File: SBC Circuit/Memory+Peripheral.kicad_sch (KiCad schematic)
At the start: 15 parts, among them U11 MCM6206CP, U12 28C256, U13 MCM6206CP, U14 28C256, U2 68681

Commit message: Small changes to prepare for review
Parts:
- renumbered C15 to C1, C16 to C2, C17 to C3, C18 to C4, C19 to C5, C20 to C6, C21 to C7, C22 to C8, U11 to U4, U12 to U5, U13 to U6, U14 to U7

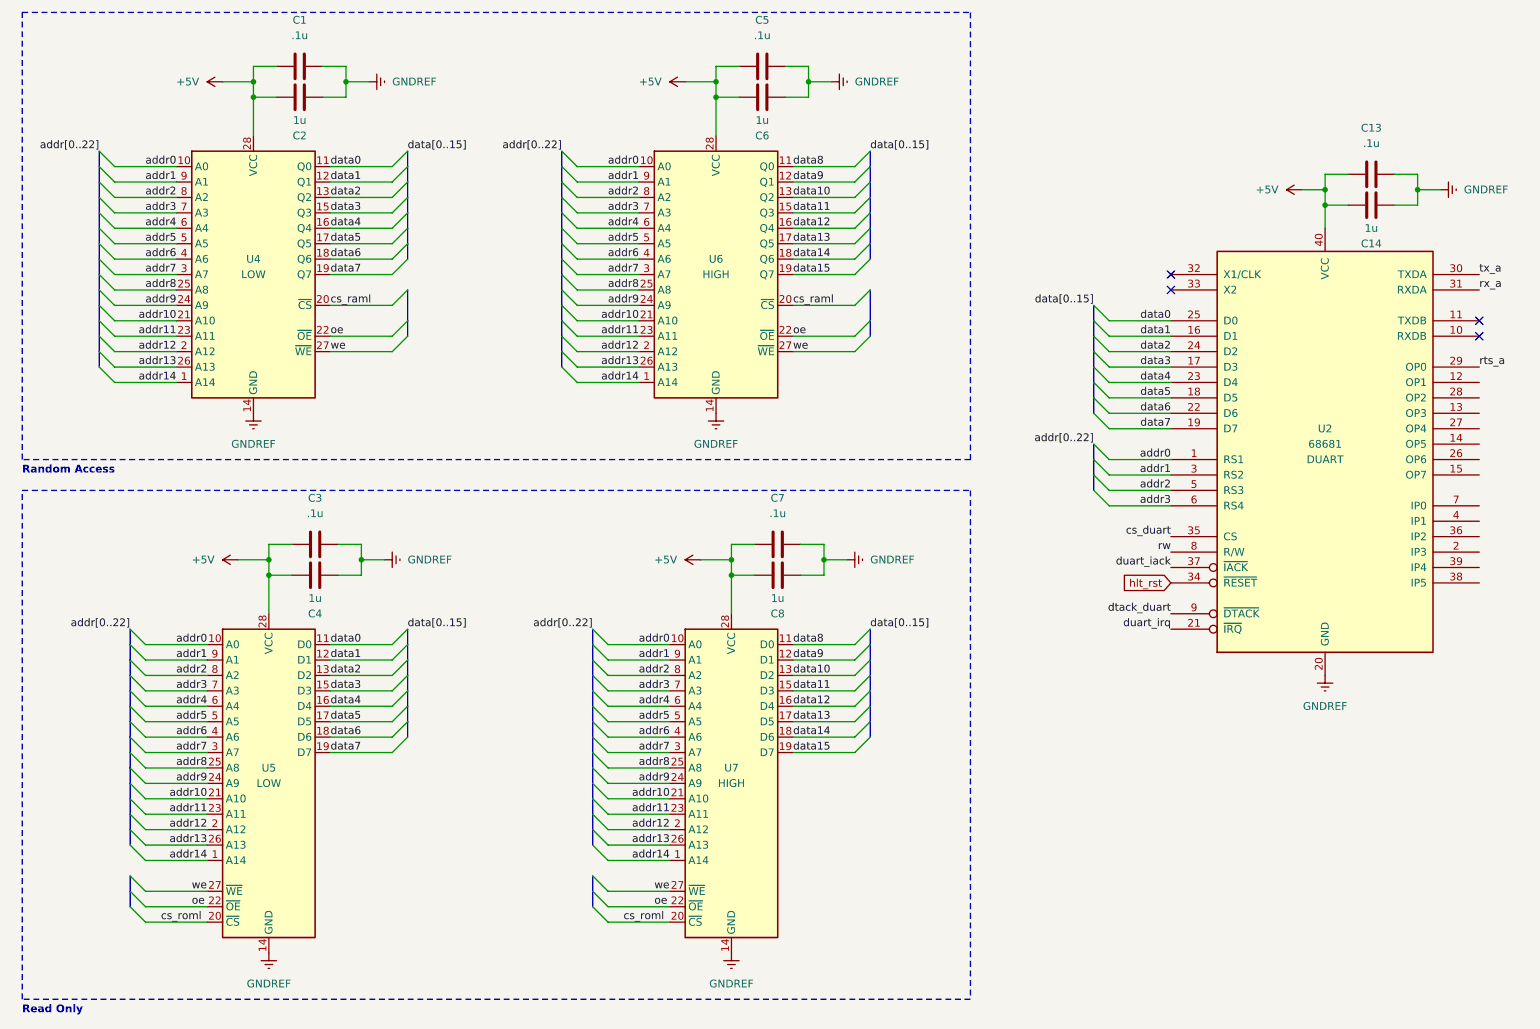
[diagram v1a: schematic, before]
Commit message: New part selections, serial port selection
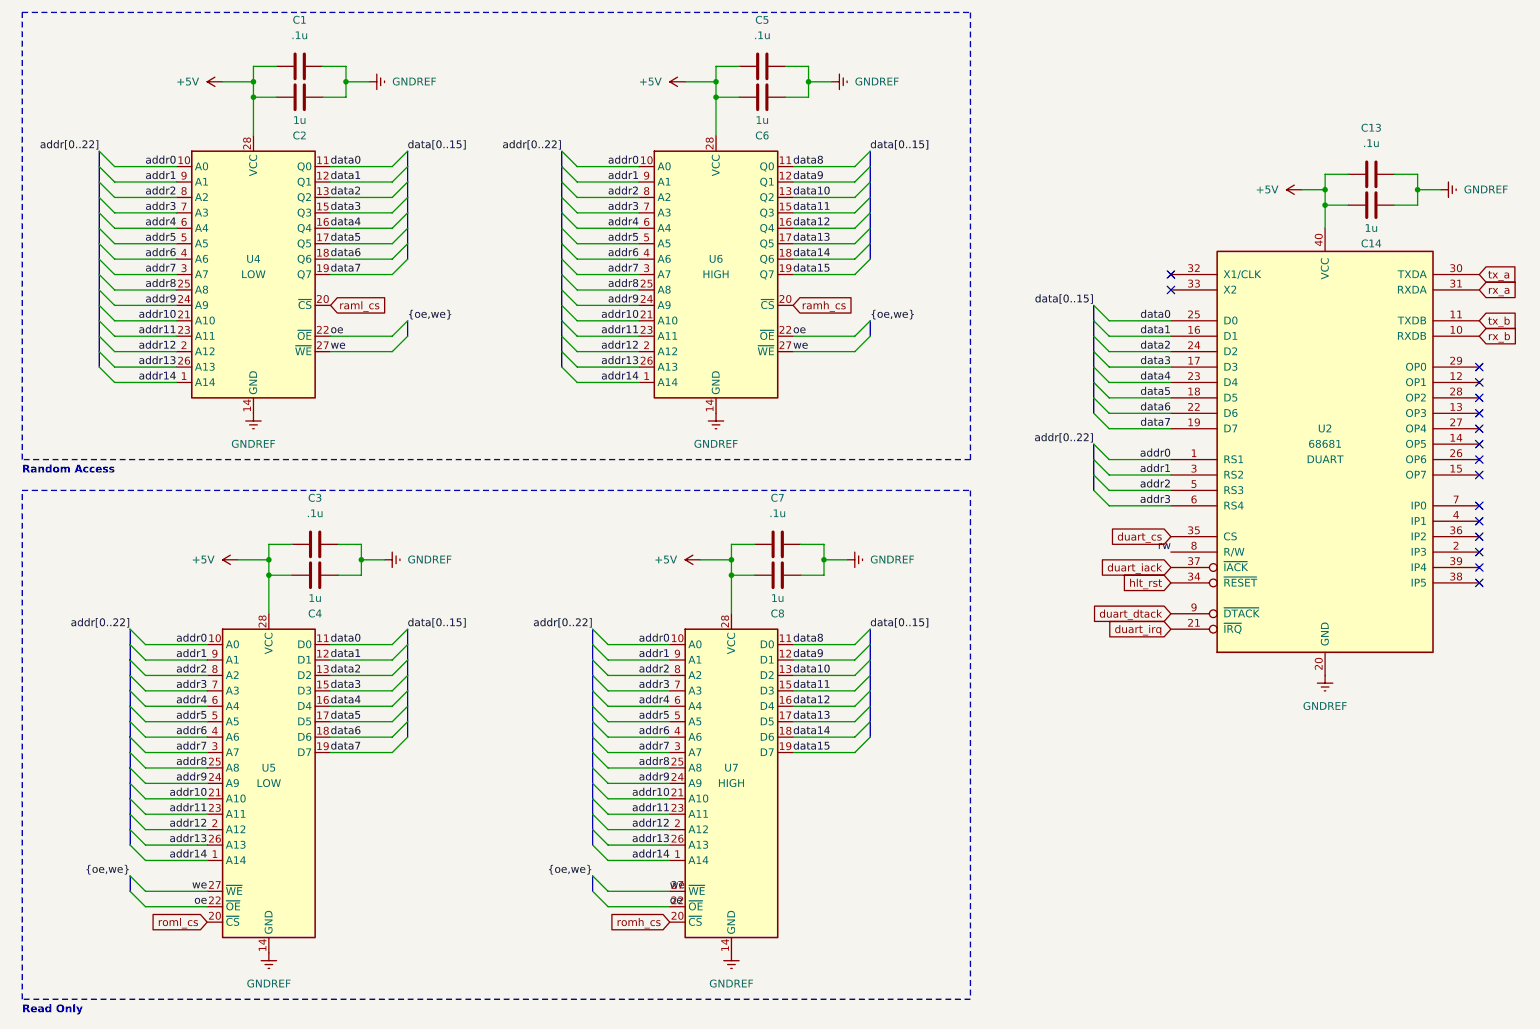
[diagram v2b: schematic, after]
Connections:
- net rx_b: now reaches U2.10 (RXDB)
- net tx_b: now reaches U2.11 (TXDB)
- net cs_duart renamed duart_cs
- net cs_raml renamed ramh_cs
- net ramh_cs: no longer U4.20 (~{CS})
- net cs_roml renamed romh_cs
- net romh_cs: no longer U5.20 (~{CS})
- net dtack_duart renamed duart_dtack
- net rts_a: no longer names the net of U2.29 (OP0)
- new net raml_cs: U4.20 (~{CS})
- new net roml_cs: U5.20 (~{CS})
- no-connect marks 4 -> 16
